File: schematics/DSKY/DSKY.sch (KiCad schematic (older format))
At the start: 0 parts

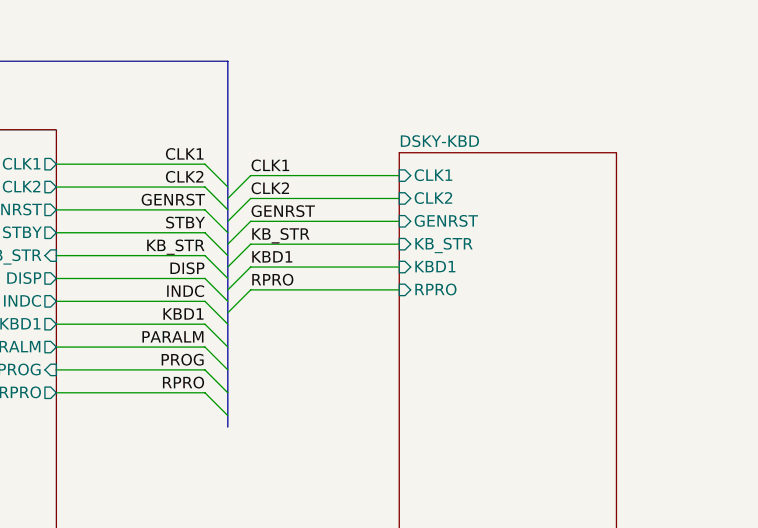
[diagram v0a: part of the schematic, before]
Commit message: Minor tweaks to the display decoding logic.
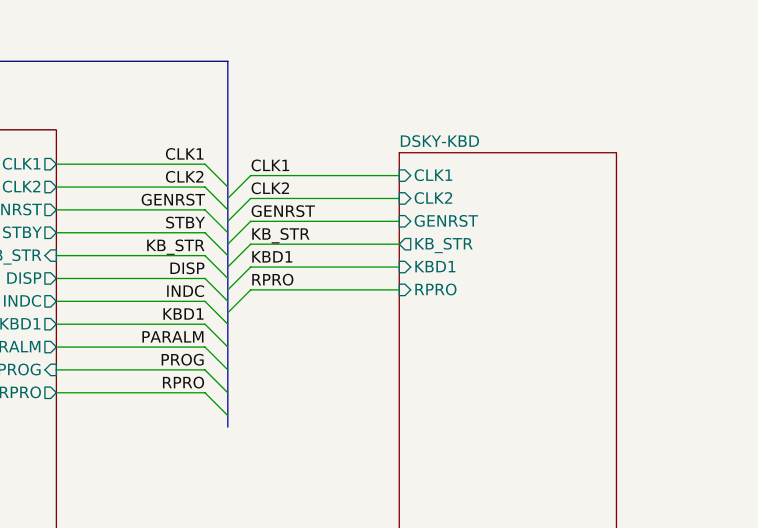
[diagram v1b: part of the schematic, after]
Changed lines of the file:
@@
 F2 "CLK2" I L 8100 3350 50
 F3 "GENRST" I L 8100 3450 50
-F4 "KB_STR" I L 8100 3550 50
+F4 "KB_STR" O L 8100 3550 50
 F5 "CH[1..5]" O L 8100 4950 50
 F6 "KBD1" I L 8100 3650 50

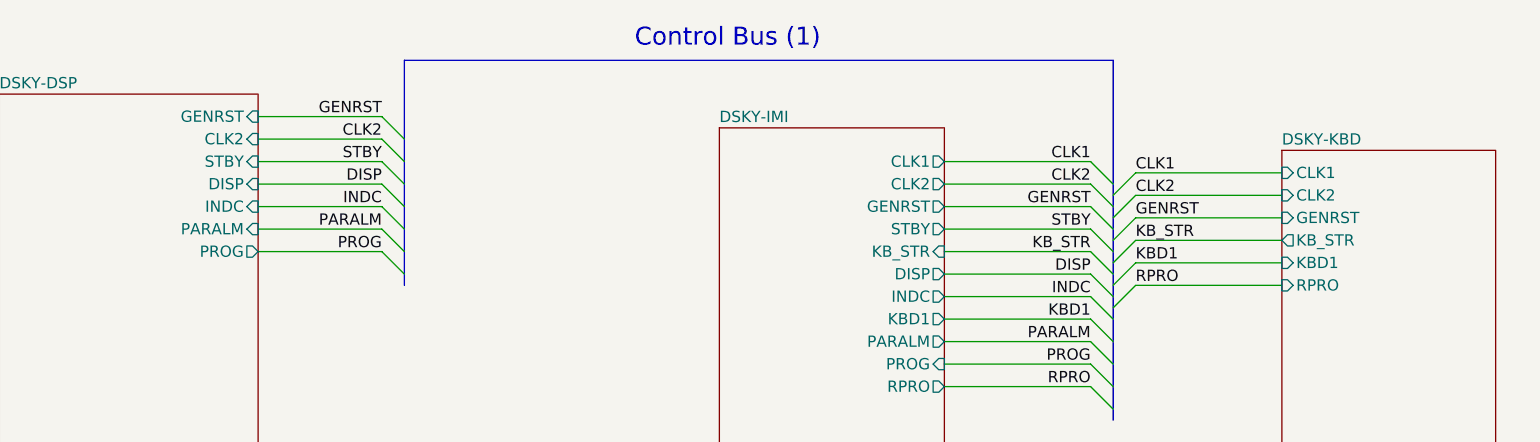
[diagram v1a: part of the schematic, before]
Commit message: Simplified reset lines.
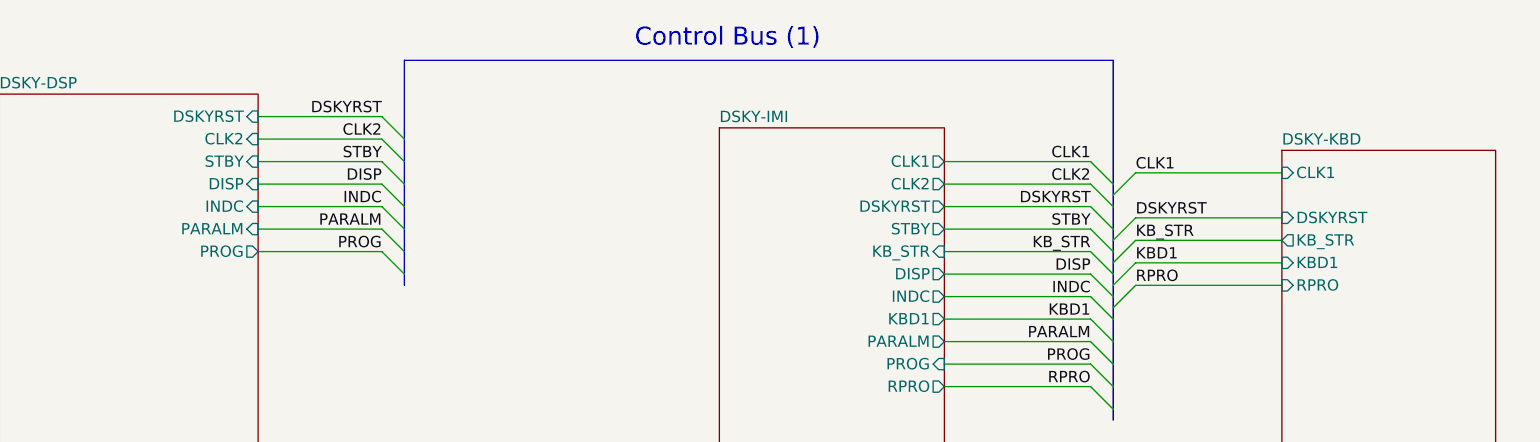
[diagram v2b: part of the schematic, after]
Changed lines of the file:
@@
 	8100 3450 7450 3450
 Text Label 7450 3450 0    50   ~ 0
-GENRST
+DSKYRST
 Text Label 7250 3400 2    50   ~ 0
-GENRST
-Entry Wire Line
-	7350 3450 7450 3350
-Text Label 7450 3350 0    50   ~ 0
-CLK2
+DSKYRST
 Wire Wire Line
 	6600 3300 7250 3300
@@
 CLK2
 Text Label 4100 3000 2    50   ~ 0
-GENRST
+DSKYRST
 Text Label 4100 3300 2    50   ~ 0
 DISP
-Wire Wire Line
-	8100 3350 7450 3350
 Wire Wire Line
 	3550 3000 4100 3000
@@
 F0 "DSKY-DSP" 50
 F1 "DSKY-DSP.sch" 50
-F2 "GENRST" I R 3550 3000 50
+F2 "DSKYRST" I R 3550 3000 50
 F3 "CLK2" I R 3550 3100 50
 F4 "CH[1..15]" I R 3550 5100 50
@@
 F1 "DSKY-IMI.sch" 50
 F2 "CLK2" O R 6600 3300 50
-F3 "GENRST" O R 6600 3400 50
+F3 "DSKYRST" O R 6600 3400 50
 F4 "CLK1" O R 6600 3200 50
 F5 "STBY" O R 6600 3500 50
@@
 F0 "DSKY-KBD" 50
 F1 "DSKY-KBD.sch" 50
-F2 "CLK2" I L 8100 3350 50
-F3 "GENRST" I L 8100 3450 50
-F4 "KB_STR" O L 8100 3550 50
-F5 "CH[1..5]" O L 8100 4950 50
-F6 "KBD1" I L 8100 3650 50
-F7 "CLK1" I L 8100 3250 50
-F8 "CH[14..14]" O L 8100 5050 50
-F9 "RPRO" I L 8100 3750 50
+F2 "DSKYRST" I L 8100 3450 50
+F3 "KB_STR" O L 8100 3550 50
+F4 "CH[1..5]" O L 8100 4950 50
+F5 "KBD1" I L 8100 3650 50
+F6 "CLK1" I L 8100 3250 50
+F7 "CH[14..14]" O L 8100 5050 50
+F8 "RPRO" I L 8100 3750 50
 $EndSheet
 Entry Wire Line

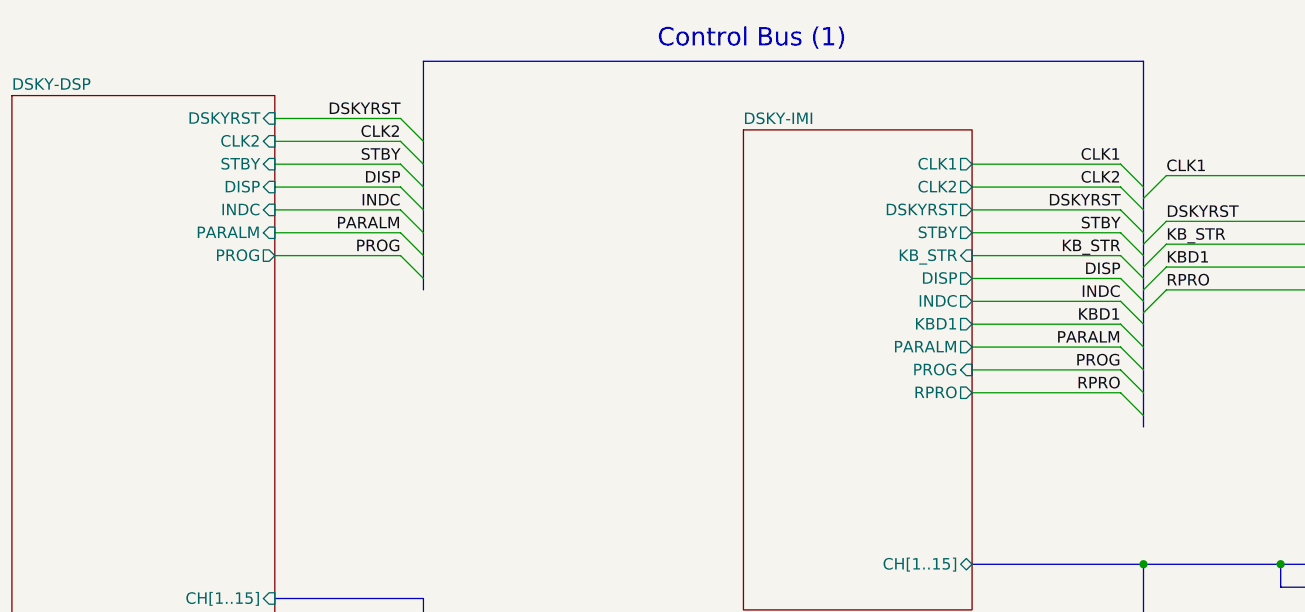
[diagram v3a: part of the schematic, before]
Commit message: Overhauled the handling of the sign characters.
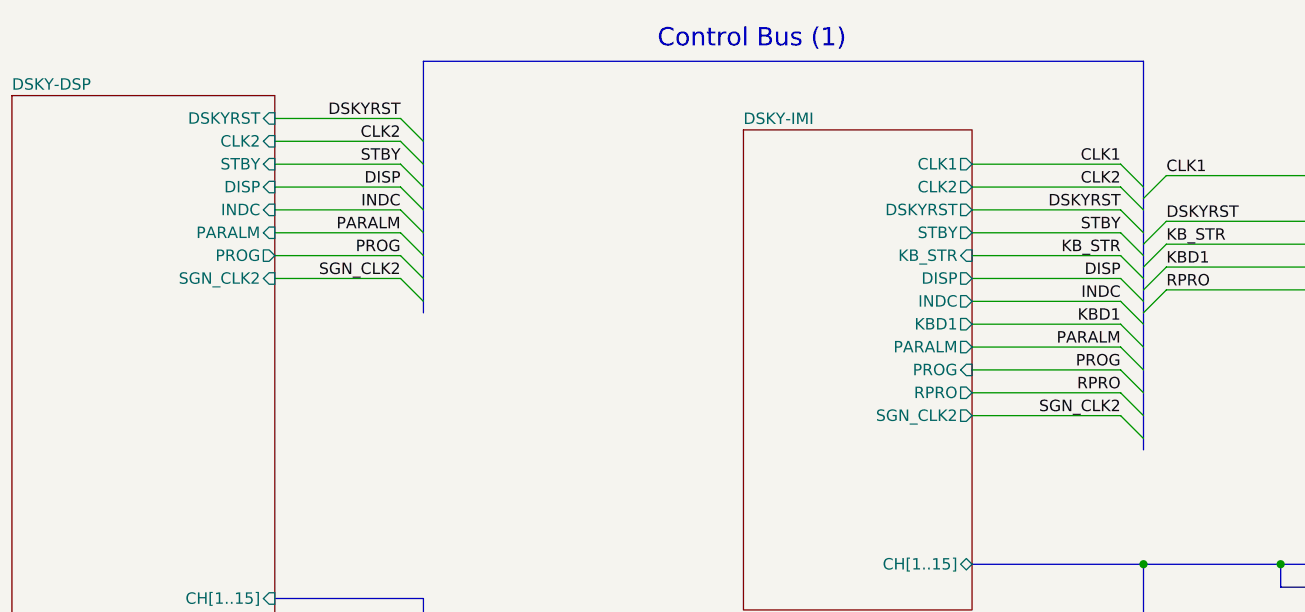
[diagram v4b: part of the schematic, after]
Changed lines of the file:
@@
 F8 "INDC" I R 3550 3400 50
 F9 "PROG" O R 3550 3600 50
+F10 "SGN_CLK2" I R 3550 3700 50
 $EndSheet
 $Sheet
@@
 F12 "PROG" I R 6600 4100 50
 F13 "RPRO" O R 6600 4200 50
+F14 "SGN_CLK2" O R 6600 4300 50
 $EndSheet
 Wire Wire Line
@@
 Wire Wire Line
 	8100 3750 7450 3750
+Wire Wire Line
+	6600 4300 7250 4300
+Entry Wire Line
+	7250 4300 7350 4400
+Text Label 7250 4300 2    50   ~ 0
+SGN_CLK2
+Entry Wire Line
+	4200 3800 4100 3700
+Text Label 4100 3700 2    50   ~ 0
+SGN_CLK2
+Wire Wire Line
+	3550 3700 4100 3700
 Wire Bus Line
-	4200 2750 4200 3750
+	4200 2750 4200 3850
 Wire Bus Line
-	7350 2750 7350 4350
+	7350 2750 7350 4450
 $EndSCHEMATC

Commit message: Final tweaks, the DSKY is now complete!
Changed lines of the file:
@@
 F9 "PROG" O R 3550 3600 50
 F10 "SGN_CLK2" I R 3550 3700 50
+F11 "CLK3" I R 3550 3800 50
 $EndSheet
 $Sheet
@@
 F13 "RPRO" O R 6600 4200 50
 F14 "SGN_CLK2" O R 6600 4300 50
+F15 "CLK3" O R 6600 4400 50
 $EndSheet
 Wire Wire Line
@@
 Wire Wire Line
 	3550 3700 4100 3700
+Wire Wire Line
+	6600 4400 7250 4400
+Entry Wire Line
+	7250 4400 7350 4500
+Text Label 7250 4400 2    50   ~ 0
+CLK3
+Entry Wire Line
+	4200 3900 4100 3800
+Text Label 4100 3800 2    50   ~ 0
+CLK3
+Wire Wire Line
+	3550 3800 4100 3800
 Wire Bus Line
-	4200 2750 4200 3850
+	4200 2750 4200 3950
 Wire Bus Line
-	7350 2750 7350 4450
+	7350 2750 7350 4550
 $EndSCHEMATC

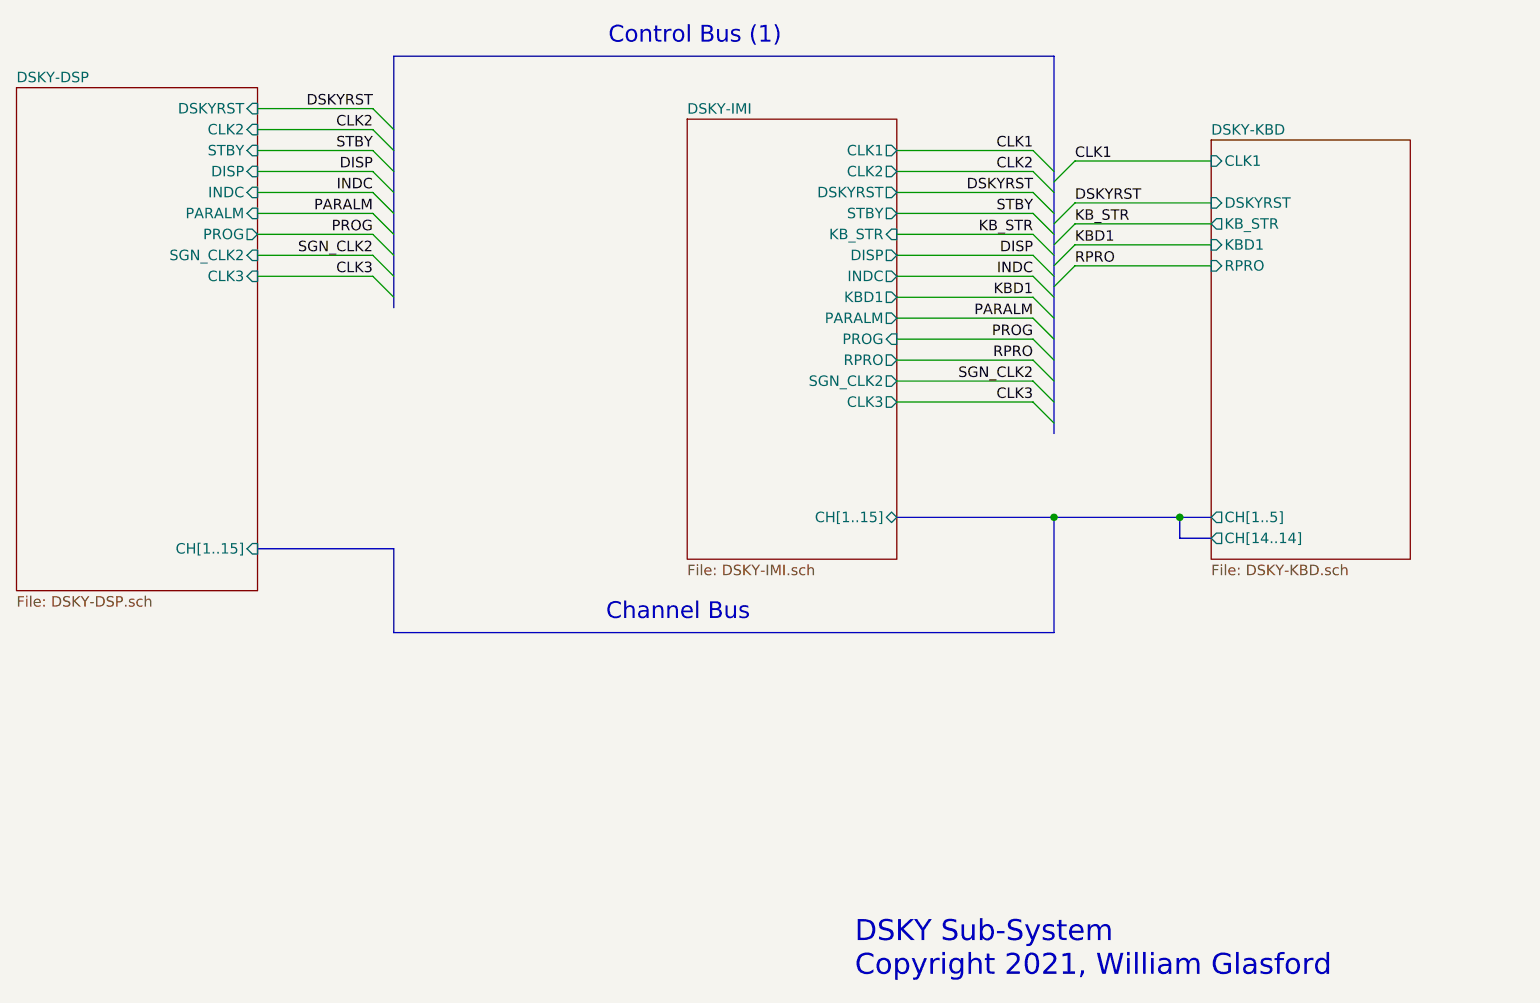
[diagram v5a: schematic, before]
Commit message: Added DSKY test schematic
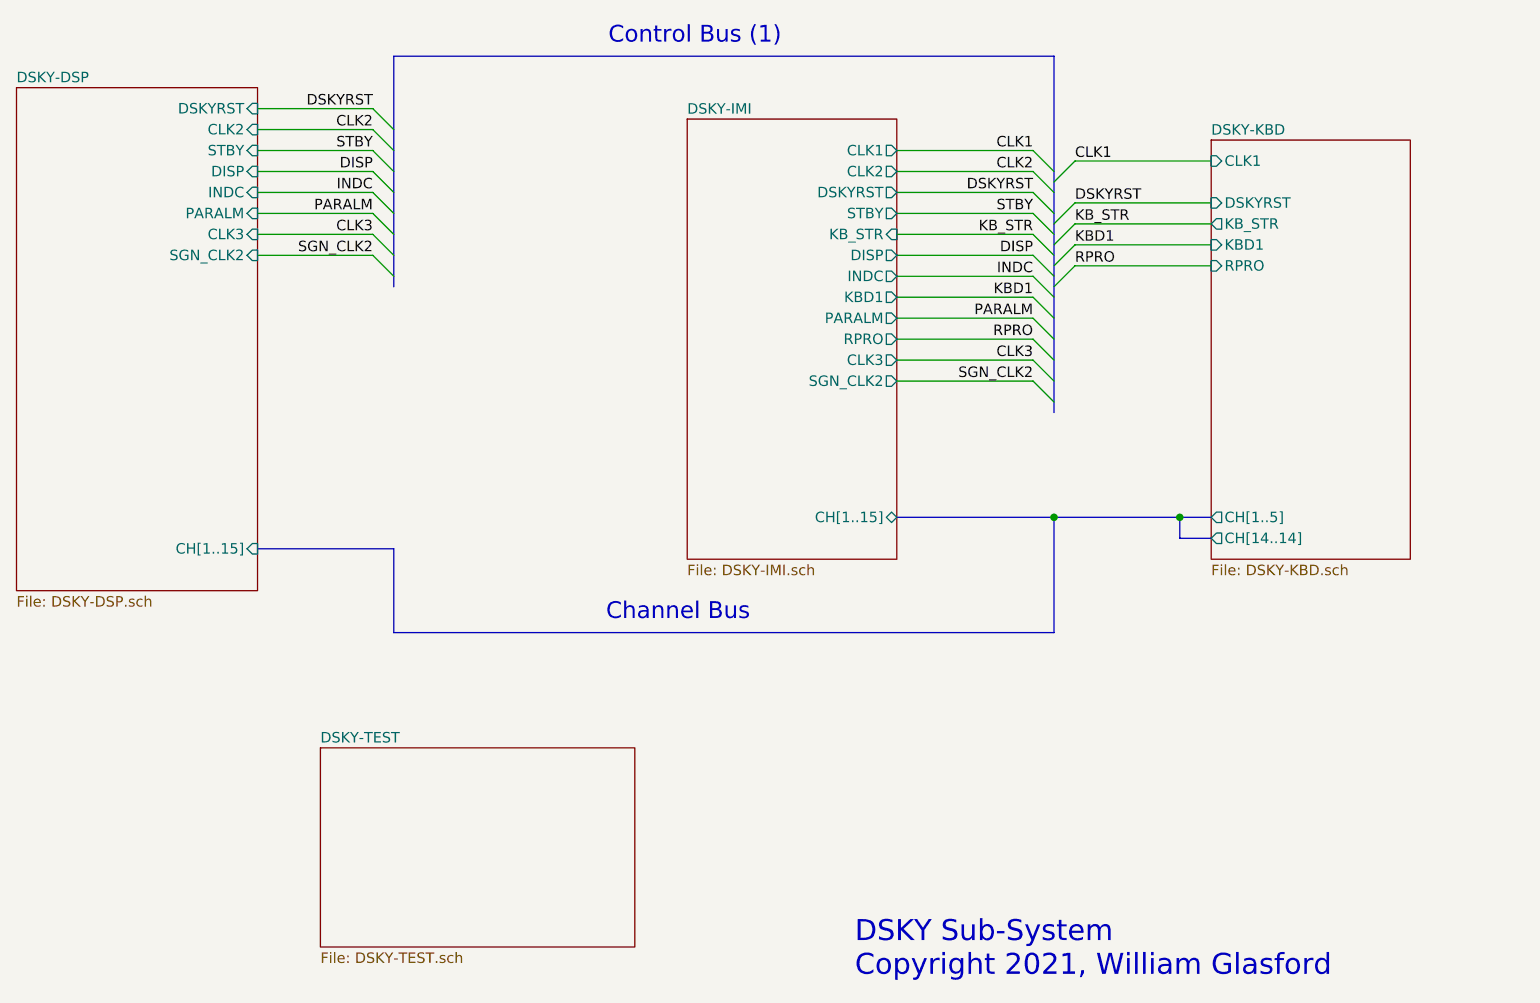
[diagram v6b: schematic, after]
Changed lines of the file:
@@
 $Descr A 11000 8500
 encoding utf-8
-Sheet 1 11
+Sheet 1 12
 Title ""
 Date ""
@@
 F7 "DISP" I R 3550 3300 50
 F8 "INDC" I R 3550 3400 50
-F9 "PROG" O R 3550 3600 50
-F10 "SGN_CLK2" I R 3550 3700 50
-F11 "CLK3" I R 3550 3800 50
+F9 "SGN_CLK2" I R 3550 3700 50
+F10 "CLK3" I R 3550 3600 50
 $EndSheet
 $Sheet
@@
 F10 "DISP" O R 6600 3700 50
 F11 "INDC" O R 6600 3800 50
-F12 "PROG" I R 6600 4100 50
-F13 "RPRO" O R 6600 4200 50
-F14 "SGN_CLK2" O R 6600 4300 50
-F15 "CLK3" O R 6600 4400 50
+F12 "RPRO" O R 6600 4100 50
+F13 "SGN_CLK2" O R 6600 4300 50
+F14 "CLK3" O R 6600 4200 50
 $EndSheet
 Wire Wire Line
@@
 Entry Wire Line
 	7250 4100 7350 4200
+Entry Wire Line
+	4200 3700 4100 3600
+Wire Wire Line
+	3550 3600 4100 3600
+Wire Wire Line
+	6600 4200 7250 4200
+Entry Wire Line
+	7250 4200 7350 4300
 Text Label 7250 4100 2    50   ~ 0
-PROG
-Entry Wire Line
-	4200 3700 4100 3600
-Text Label 4100 3600 2    50   ~ 0
-PROG
-Wire Wire Line
-	3550 3600 4100 3600
-Wire Wire Line
-	6600 4200 7250 4200
-Entry Wire Line
-	7250 4200 7350 4300
-Text Label 7250 4200 2    50   ~ 0
 RPRO
 Entry Wire Line
@@
 Wire Wire Line
 	3550 3700 4100 3700
-Wire Wire Line
-	6600 4400 7250 4400
-Entry Wire Line
-	7250 4400 7350 4500
-Text Label 7250 4400 2    50   ~ 0
+Text Label 7250 4200 2    50   ~ 0
 CLK3
-Entry Wire Line
-	4200 3900 4100 3800
-Text Label 4100 3800 2    50   ~ 0
+Text Label 4100 3600 2    50   ~ 0
 CLK3
-Wire Wire Line
-	3550 3800 4100 3800
-Wire Bus Line
-	4200 2750 4200 3950
-Wire Bus Line
-	7350 2750 7350 4550
+$Sheet
+S 3850 6050 1500 950
+U 62ECFB9F
+F0 "DSKY-TEST" 50
+F1 "DSKY-TEST.sch" 50
+$EndSheet
+Wire Bus Line
+	4200 2750 4200 3850
+Wire Bus Line
+	7350 2750 7350 4450
 $EndSCHEMATC
